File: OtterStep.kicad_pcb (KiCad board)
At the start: 4 copper layers, 68.4 x 50 mm, 63 parts, among them J1 USB, J2 PWR, J3 IN, J4 OUT, J5 ENC, SW1 SW_Push, U1 STUSB4500, U2 USBLC6-4, U3 powerSTEP01, U4 SE8633X2-HF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

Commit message: updated files
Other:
- board text added: "github.com/Jan--Henrik/OtterStepMini @JanHenrikH 2021"

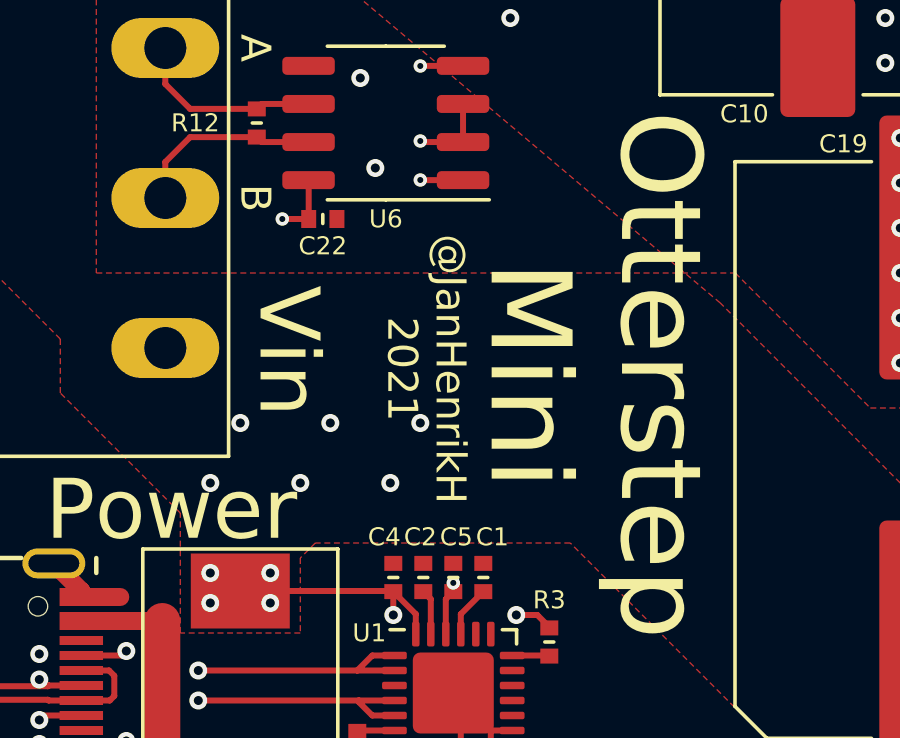
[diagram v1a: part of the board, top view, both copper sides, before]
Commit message: changed silk
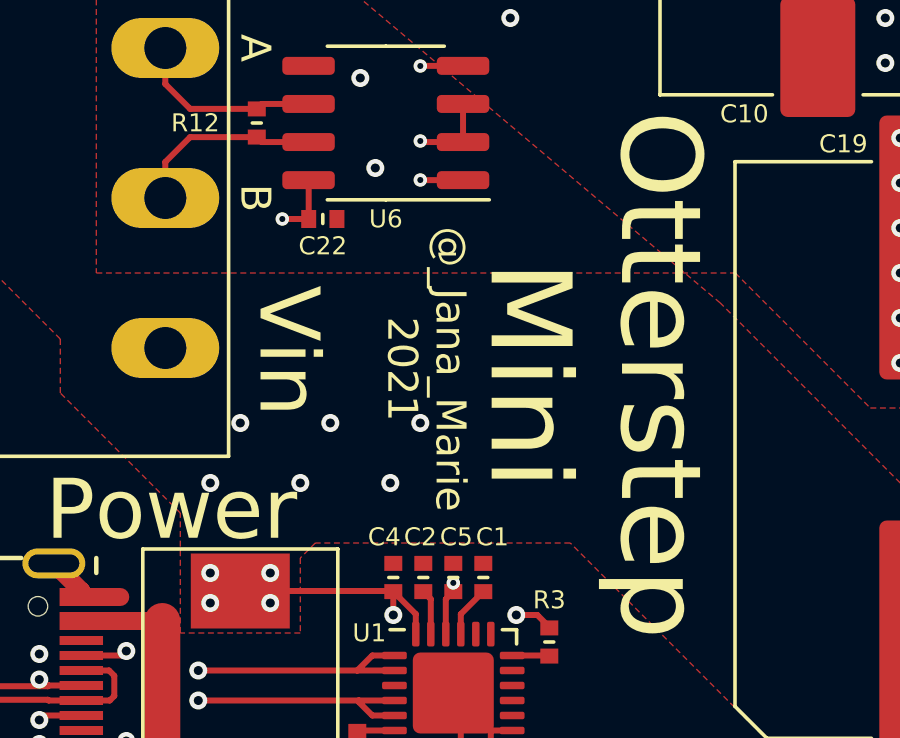
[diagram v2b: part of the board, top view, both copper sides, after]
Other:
- board text added: "@_Jana_Marie 2021"
- board text added: "github.com/Jana-Marie/OtterStepMini @_Jana_Marie 2021"
- board text removed: "@JanHenrikH 2021"
- board text removed: "github.com/Jan--Henrik/OtterStepMini @JanHenrikH 2021"
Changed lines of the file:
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@@
     )
   )
-  (gr_text "github.com/Jan--Henrik/OtterStepMini\n@JanHenrikH  2021" (at 66.4 75 270) (layer B.SilkS)
+  (gr_text "github.com/Jana-Marie/OtterStepMini\n@_Jana_Marie  2021" (at 66.4 75 270) (layer B.SilkS)
     (effects (font (size 1.3 1.3) (thickness 0.13)) (justify mirror))
   )
-  (gr_text "@JanHenrikH\n2021" (at 69.2 83.2 270) (layer F.SilkS)
+  (gr_text "@_Jana_Marie\n2021" (at 69.2 83.2 270) (layer F.SilkS)
     (effects (font (size 1 1) (thickness 0.12)))
   )
